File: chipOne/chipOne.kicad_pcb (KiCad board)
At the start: 2 copper layers, 120 x 110 mm, 27 parts, among them J1 BNC, J2 BNC, J3 5767007-8, J4 5767007-8, U1 Y1247AstimulusGenerator, U10A1 3pinSwitchCustom, U2 Y1247AstimulusGenerator, U3 Y1247AstimulusGenerator, U4 Y1247AstimulusGenerator, U5 CHIP1, U6 3pinSwitchCustom

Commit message: Combined both the boards
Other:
- copper layers 2 -> 4

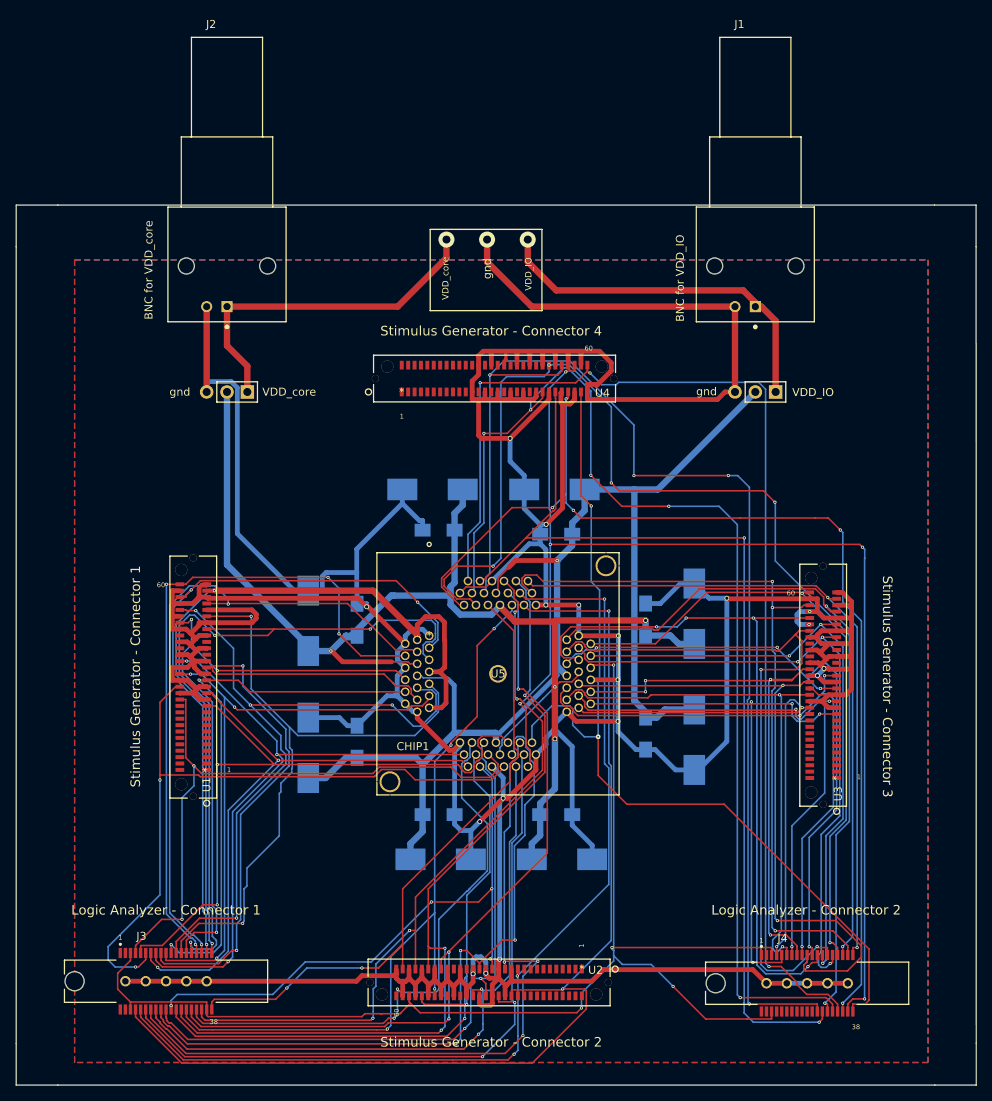
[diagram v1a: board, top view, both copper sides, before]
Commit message: Switch changed in both the layout
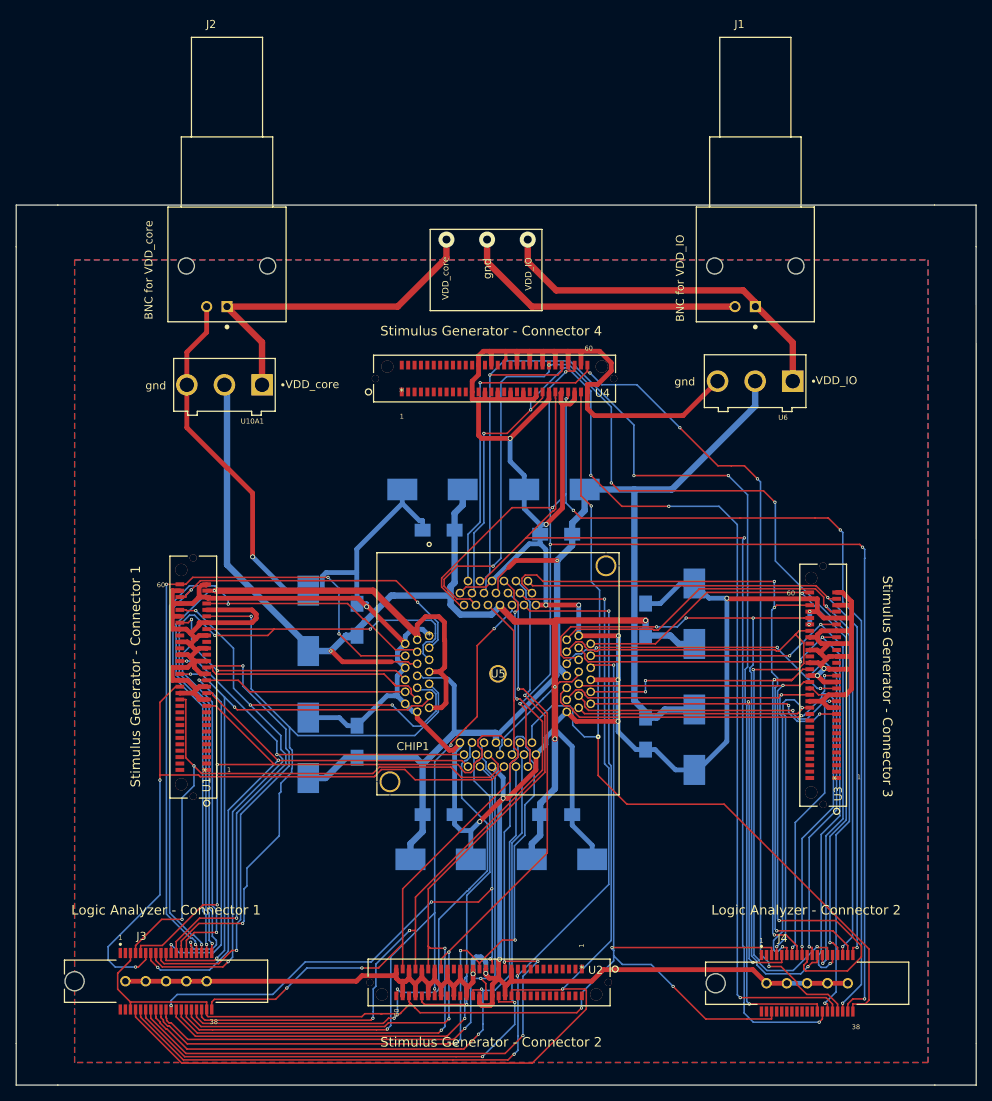
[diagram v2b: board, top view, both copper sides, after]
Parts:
- U10A1, U6: footprint Pin_Headers:Pin_Header_Straight_1x03_Pitch2.54mm -> SW_MS12ANW03:SW_MS12ANW03
- moved U10A1 3.00 mm to (47.9, 62.6), turned to 180 degrees
- moved U6 2.89 mm to (114.3, 62.1), turned to 180 degrees
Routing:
- net VSSQ: track 769.3 -> 755.0 mm, vias 19 -> 20
- net I_address1: track 147.6 -> 140.2 mm, vias 3 -> 5
- net VDD_IO: track 161.7 -> 164.1 mm
- net B_inData_bi7: track 89.8 -> 91.6 mm
- net VDD_core: track 167.3 -> 168.4 mm
- net B_outData_bi1: track 69.3 -> 68.3 mm
- net Net-(J1-Pad1): track 46.0 -> 45.2 mm
- net B_outData_bi5: track 63.9 -> 64.7 mm
- net I_address5: track 155.1 -> 154.5 mm

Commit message: Testing for all connections in Chip One is Completed
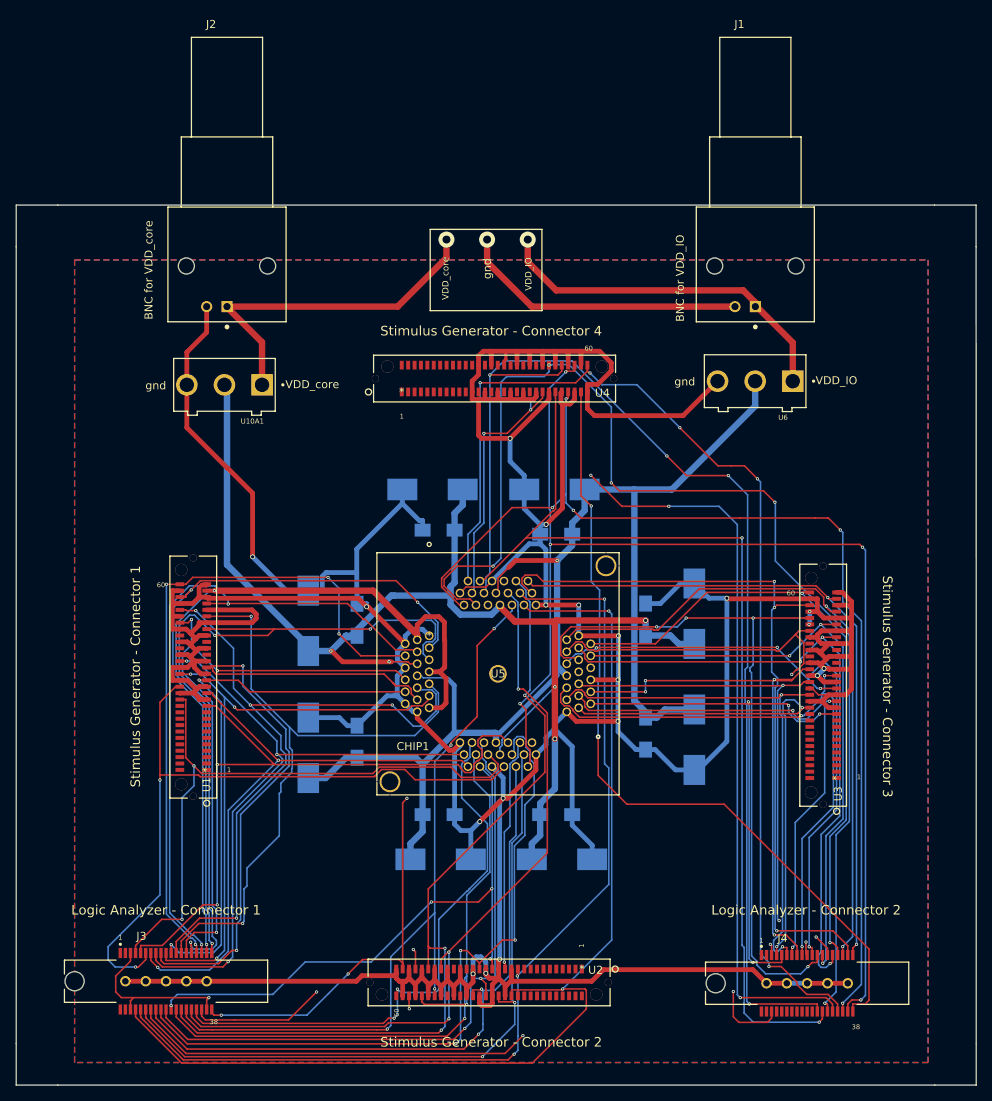
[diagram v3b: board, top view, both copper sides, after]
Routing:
- net B_inData_bi11: track 82.6 -> 66.2 mm, vias 2 -> 3
- net VDD_core: track 168.4 -> 183.2 mm, vias 4 -> 5
- net B_inData_bi7: track 91.6 -> 76.8 mm
- net I_clk: track 162.4 -> 148.5 mm
- net I_address2: track 145.5 -> 135.8 mm
- net B_outData_bi6: track 115.6 -> 110.5 mm
- net VSSQ: track 755.0 -> 759.6 mm
- net O_outData6: track 93.9 -> 89.8 mm, vias 3 -> 2
- net I_address5: track 154.5 -> 150.8 mm
- net I_reset: track 81.0 -> 78.1 mm, vias 2 -> 3
- net I_inData0: track 93.9 -> 92.7 mm, vias 4 -> 2

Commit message: Checking for chip two completed, Combined PCB updated
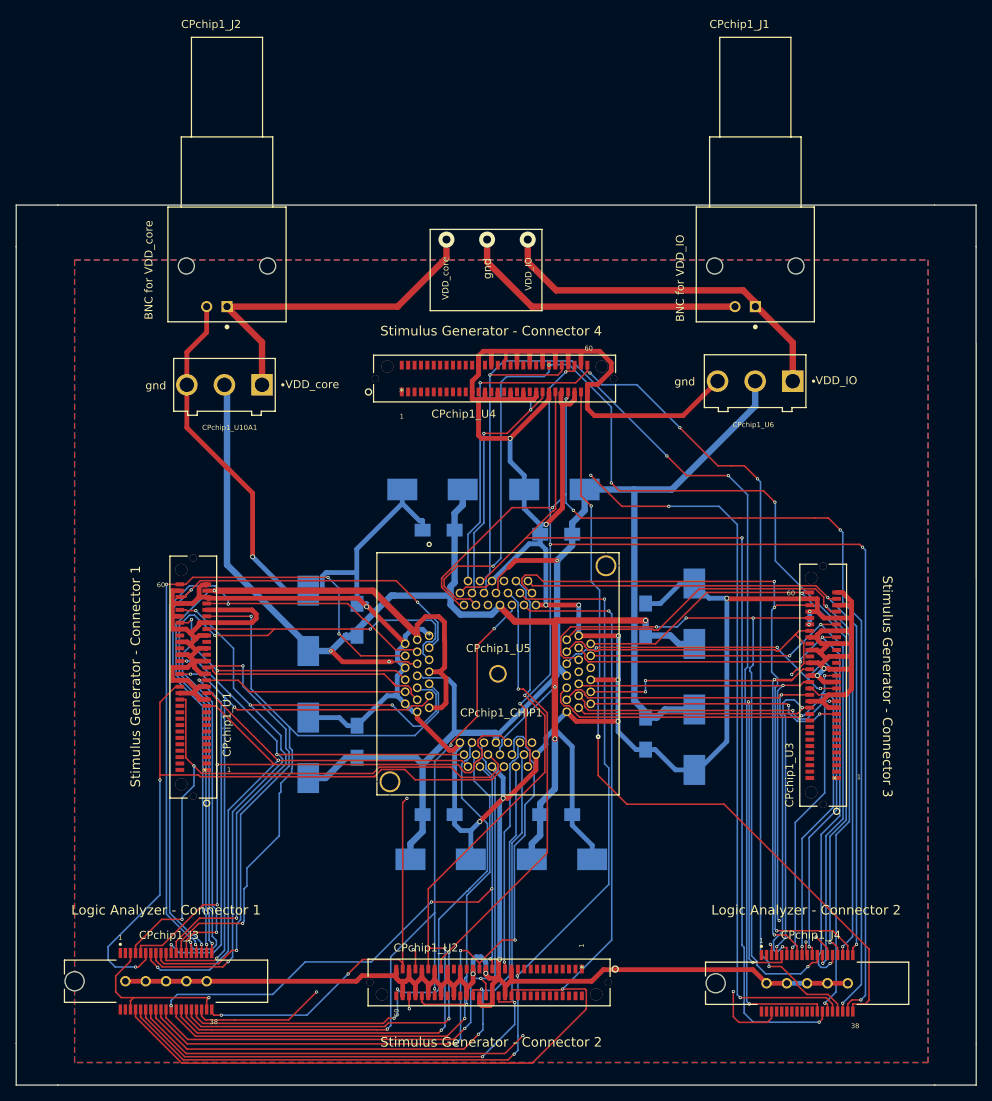
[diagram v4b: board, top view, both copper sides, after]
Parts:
- CPchip1_U5: renamed from U5; value CHIP1 -> CPchip1_CHIP1
- renumbered C1 to CPchip1_C1, C10 to CPchip1_C10, C11 to CPchip1_C11, C12 to CPchip1_C12, C13 to CPchip1_C13, C14 to CPchip1_C14, C15 to CPchip1_C15, C16 to CPchip1_C16, C2 to CPchip1_C2, C3 to CPchip1_C3, C4 to CPchip1_C4, C5 to CPchip1_C5, C6 to CPchip1_C6, C7 to CPchip1_C7, C8 to CPchip1_C8, C9 to CPchip1_C9, J1 to CPchip1_J1, J2 to CPchip1_J2, J3 to CPchip1_J3, J4 to CPchip1_J4, U1 to CPchip1_U1, U10A1 to CPchip1_U10A1, U2 to CPchip1_U2, U3 to CPchip1_U3, U4 to CPchip1_U4, U6 to CPchip1_U6

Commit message: Both Chips final modification done
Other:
- board size 120 x 110 mm -> 113 x 109 mm
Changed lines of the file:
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@@
   (general
     (thickness 1.6)
-    (drawings 44)
+    (drawings 37)
     (tracks 2010)
     (zones 0)
@@
   (module Y1247AstimulusGenerator:ERF8-030-05.0-L-DV-L-TR (layer F.Cu)
     (at 45.72 110.744 270)
-    (fp_text reference CPchip1_U1 (at -5.669 -2.53 90) (layer F.SilkS)
+    (fp_text reference CPchip1_U1 (at -5.744 1.72 90) (layer F.SilkS)
       (effects (font (size 1 1) (thickness 0.15)))
     )
@@
   (module Y1247AstimulusGenerator:ERF8-030-05.0-L-DV-L-TR (layer F.Cu)
     (at 92.6211 135.636)
-    (fp_text reference CPchip1_U2 (at -19.4961 -2.661) (layer F.SilkS)
+    (fp_text reference CPchip1_U2 (at -18.6211 1.764) (layer F.SilkS)
       (effects (font (size 1 1) (thickness 0.15)))
     )
@@
   (module Y1247AstimulusGenerator:ERF8-030-05.0-L-DV-L-TR (layer F.Cu)
     (at 70.104 63.5 180)
-    (fp_text reference CPchip1_U4 (at -7.746 -2.75) (layer F.SilkS)
+    (fp_text reference CPchip1_U4 (at -6.896 1.5) (layer F.SilkS)
       (effects (font (size 1 1) (thickness 0.15)))
     )
@@
   (module Y1247AstimulusGenerator:ERF8-030-05.0-L-DV-L-TR (layer F.Cu)
     (at 124.46 111.76 270)
-    (fp_text reference CPchip1_U3 (at -0.385 5.885 90) (layer F.SilkS)
+    (fp_text reference CPchip1_U3 (at -2.76 1.46 90) (layer F.SilkS)
       (effects (font (size 1 1) (thickness 0.15)))
     )
@@
   (module U4164AlogicAnalyser:TE_5767007-8 (layer F.Cu)
     (at 40.64 137.16)
-    (fp_text reference CPchip1_J3 (at 0.36 -5.76) (layer F.SilkS)
+    (fp_text reference CPchip1_J3 (at 0.36 -2.16) (layer F.SilkS)
       (effects (font (size 1.000346 1.000346) (thickness 0.250087)))
     )
@@
   (module U4164AlogicAnalyser:TE_5767007-8 (layer F.Cu)
     (at 120.777 137.414)
-    (fp_text reference CPchip1_J4 (at 0.448 -6.039) (layer F.SilkS)
+    (fp_text reference CPchip1_J4 (at 0.223 -1.814) (layer F.SilkS)
       (effects (font (size 1.000346 1.000346) (thickness 0.250087)))
     )
@@
   (module SW_MS12ANW03:SW_MS12ANW03 (layer F.Cu)
     (at 114.28 62.15 180)
-    (fp_text reference CPchip1_U6 (at 0.23 -5.45) (layer F.SilkS)
+    (fp_text reference CPchip1_U6 (at 0.28 -2.45) (layer F.SilkS)
       (effects (font (size 0.64 0.64) (thickness 0.16)))
     )
@@
   (module SW_MS12ANW03:SW_MS12ANW03 (layer F.Cu)
     (at 47.94 62.61 180)
-    (fp_text reference CPchip1_U10A1 (at -0.66 -5.34) (layer F.SilkS)
+    (fp_text reference CPchip1_U10A1 (at -0.26 -2.39) (layer F.SilkS)
       (effects (font (size 0.64 0.64) (thickness 0.16)))
     )
@@
       (net 2 VSSQ))
   )
+  (gr_line (start 25 40) (end 25 149) (layer Edge.Cuts) (width 0.05))
+  (gr_line (start 32 40) (end 25 40) (layer Edge.Cuts) (width 0.05))
+  (gr_line (start 138 40) (end 32 40) (layer Edge.Cuts) (width 0.05))
+  (gr_line (start 138 149) (end 138 40) (layer Edge.Cuts) (width 0.05))
+  (gr_line (start 25 149) (end 138 149) (layer Edge.Cuts) (width 0.05))
   (gr_text gnd (at 105.48 62.22) (layer F.SilkS)
     (effects (font (size 1 1) (thickness 0.2)))
@@
     (effects (font (size 1 1) (thickness 0.25)))
   )
-  (gr_line (start 21.91 150.14) (end 27.11 150.14) (layer Edge.Cuts) (width 0.05))
-  (gr_line (start 21.91 144.94) (end 21.91 150.14) (layer Edge.Cuts) (width 0.05))
-  (gr_line (start 21.91 40.14) (end 27.11 40.14) (layer Edge.Cuts) (width 0.05))
-  (gr_line (start 21.91 45.34) (end 21.91 40.14) (layer Edge.Cuts) (width 0.05))
-  (gr_line (start 141.9 40.14) (end 141.9 45.34) (layer Edge.Cuts) (width 0.05))
-  (gr_line (start 136.7 40.14) (end 141.9 40.14) (layer Edge.Cuts) (width 0.05))
-  (gr_line (start 141.92 150.14) (end 141.92 144.94) (layer Edge.Cuts) (width 0.05))
-  (gr_line (start 136.72 150.14) (end 141.92 150.14) (layer Edge.Cuts) (width 0.05))
-  (gr_text "PCB Designed for Chip 1" (at 123.825 145.415) (layer B.SilkS)
+  (gr_text "PCB Designed for Chip 1" (at 123 147) (layer B.SilkS)
     (effects (font (size 1.5 1.5) (thickness 0.3)) (justify mirror))
   )
@@
     (effects (font (size 1.2 1.2) (thickness 0.25)))
   )
-  (gr_text "Stimulus Generator - Connector 4" (at 81.28 55.88) (layer F.SilkS)
+  (gr_text "Stimulus Generator - Connector 4" (at 82 67.6) (layer F.SilkS)
     (effects (font (size 1.2 1.2) (thickness 0.25)))
   )
@@
     (effects (font (size 1.2 1.2) (thickness 0.25)))
   )
-  (gr_line (start 21.91 45.34) (end 21.91 144.94) (layer Edge.Cuts) (width 0.05))
-  (gr_line (start 27.11 40.14) (end 136.7 40.14) (layer Edge.Cuts) (width 0.05))
-  (gr_line (start 141.92 144.94) (end 141.9 45.34) (layer Edge.Cuts) (width 0.05))
-  (gr_line (start 136.72 150.14) (end 27.11 150.14) (layer Edge.Cuts) (width 0.05))
   (segment (start 81.8809 107.3279) (end 81.8809 106.171) (width 0.8) (layer B.Cu) (net 1))
   (segment (start 81.8809 107.328) (end 81.8809 107.3279) (width 0.8) (layer B.Cu) (net 1))
@@
   (segment (start 92.2274 98.740398) (end 92.2274 98.480001) (width 0.2) (layer In1.Cu) (net 3))
   (segment (start 91.233899 99.733899) (end 92.2274 98.740398) (width 0.2) (layer In1.Cu) (net 3))
-  (via (at 85.852 44.45) (size 2) (drill 1) (layers F.Cu B.Cu) (net 60))
-  (segment (start 114.3 52.832) (end 114.3 52.324) (width 0.8) (layer F.Cu) (net 60))
-  (segment (start 114.3 52.324) (end 112.776 50.8) (width 0.8) (layer F.Cu) (net 60))
-  (segment (start 112.776 50.8) (end 89.408 50.8) (width 0.8) (layer F.Cu) (net 60))
-  (segment (start 85.852 47.244) (end 85.852 44.45) (width 0.8) (layer F.Cu) (net 60))
-  (segment (start 89.408 50.8) (end 85.852 47.244) (width 0.8) (layer F.Cu) (net 60))
-  (segment (start 114.3 52.832) (end 114.482 52.832) (width 0.8) (layer F.Cu) (net 60))
-  (segment (start 118.98 57.33) (end 118.98 62.15) (width 0.8) (layer F.Cu) (net 60))
-  (segment (start 114.482 52.832) (end 118.98 57.33) (width 0.8) (layer F.Cu) (net 60))
-  (via (at 75.692 44.45) (size 2) (drill 1) (layers F.Cu B.Cu) (net 61))
-  (segment (start 75.692 46.736) (end 75.692 44.45) (width 0.8) (layer F.Cu) (net 61))
-  (segment (start 48.26 52.832) (end 69.596 52.832) (width 0.8) (layer F.Cu) (net 61))
-  (segment (start 69.596 52.832) (end 75.692 46.736) (width 0.8) (layer F.Cu) (net 61))
-  (segment (start 48.26 52.832) (end 48.26 52.91) (width 0.8) (layer F.Cu) (net 61))
-  (segment (start 52.64 57.29) (end 52.64 62.61) (width 0.8) (layer F.Cu) (net 61))
-  (segment (start 48.26 52.91) (end 52.64 57.29) (width 0.8) (layer F.Cu) (net 61))
   (segment (start 54.1833 110.07) (end 47.042 110.07) (width 0.2) (layer F.Cu) (net 4))
   (segment (start 47.042 127.6091) (end 47.042 110.07) (width 0.2) (layer B.Cu) (net 4))
@@
   (segment (start 86.2245 66.4008) (end 93.7411 73.9174) (width 0.2) (layer In1.Cu) (net 59))
   (segment (start 86.2245 65.7281) (end 86.2245 66.4008) (width 0.2) (layer In1.Cu) (net 59))
+  (via (at 85.852 44.45) (size 2) (drill 1) (layers F.Cu B.Cu) (net 60))
+  (segment (start 114.3 52.832) (end 114.3 52.324) (width 0.8) (layer F.Cu) (net 60))
+  (segment (start 114.3 52.324) (end 112.776 50.8) (width 0.8) (layer F.Cu) (net 60))
+  (segment (start 112.776 50.8) (end 89.408 50.8) (width 0.8) (layer F.Cu) (net 60))
+  (segment (start 85.852 47.244) (end 85.852 44.45) (width 0.8) (layer F.Cu) (net 60))
+  (segment (start 89.408 50.8) (end 85.852 47.244) (width 0.8) (layer F.Cu) (net 60))
+  (segment (start 114.3 52.832) (end 114.482 52.832) (width 0.8) (layer F.Cu) (net 60))
+  (segment (start 118.98 57.33) (end 118.98 62.15) (width 0.8) (layer F.Cu) (net 60))
+  (segment (start 114.482 52.832) (end 118.98 57.33) (width 0.8) (layer F.Cu) (net 60))
+  (via (at 75.692 44.45) (size 2) (drill 1) (layers F.Cu B.Cu) (net 61))
+  (segment (start 75.692 46.736) (end 75.692 44.45) (width 0.8) (layer F.Cu) (net 61))
+  (segment (start 48.26 52.832) (end 69.596 52.832) (width 0.8) (layer F.Cu) (net 61))
+  (segment (start 69.596 52.832) (end 75.692 46.736) (width 0.8) (layer F.Cu) (net 61))
+  (segment (start 48.26 52.832) (end 48.26 52.91) (width 0.8) (layer F.Cu) (net 61))
+  (segment (start 52.64 57.29) (end 52.64 62.61) (width 0.8) (layer F.Cu) (net 61))
+  (segment (start 48.26 52.91) (end 52.64 57.29) (width 0.8) (layer F.Cu) (net 61))
   (zone (net 2) (net_name VSSQ) (layer F.Cu) (hatch edge 0.508)
     (connect_pads (clearance 0.8))
@@
     (polygon
       (pts
-        (xy 135.89 147.32) (xy 29.21 147.32) (xy 29.21 46.99) (xy 135.89 46.99)
+        (xy 136 147) (xy 27 147) (xy 27 42) (xy 136 42)
       )
     )
@@
     (polygon
       (pts
-        (xy 135.89 147.32) (xy 29.21 147.32) (xy 29.21 46.99) (xy 135.89 46.99)
+        (xy 136 147) (xy 27 147) (xy 27 42) (xy 136 42)
       )
     )
